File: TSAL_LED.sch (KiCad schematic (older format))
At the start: 69 parts, among them J1 Mini-SPOX, U1 XC9141, U2 XC9141

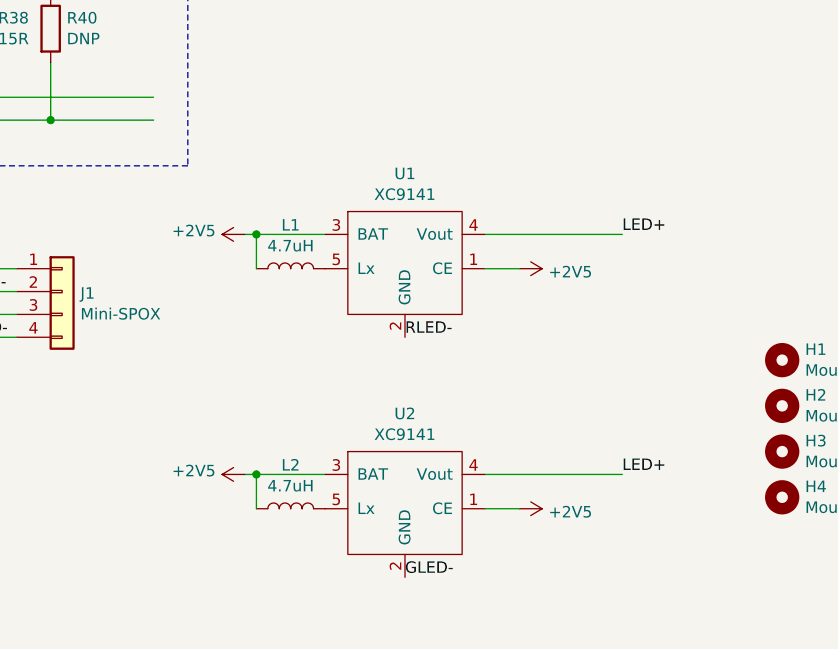
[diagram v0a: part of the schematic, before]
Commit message: remove boost converter for RLED
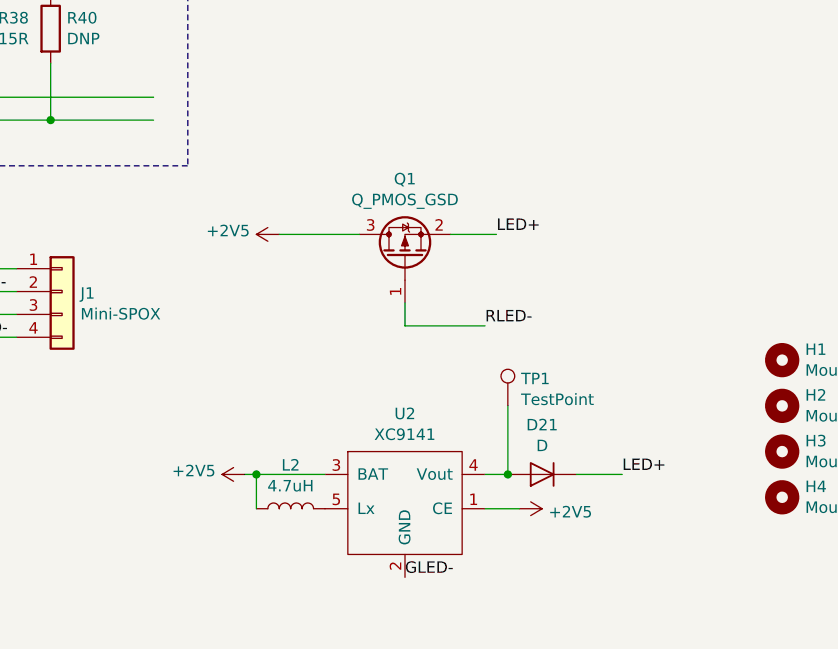
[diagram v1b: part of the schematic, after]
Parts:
- removed L1: 4.7uH, Inductor_SMD:L_Coilcraft_LPS5030, symbol Device:L
- removed U1: XC9141, Package_TO_SOT_SMD:SOT-23-5_HandSoldering, symbol xc9141:XC9141
- added D21: D, project:d0214ba, symbol Device:D
- added Q1: Q_PMOS_GSD, Package_TO_SOT_SMD:SOT-23, symbol Device:Q_PMOS_GSD
- added TP1: TestPoint, TestPoint:TestPoint_Pad_D3.0mm, symbol Connector:TestPoint
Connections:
- wire segments 146 -> 147
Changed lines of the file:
@@
-$EndComp
-$Comp
-L xc9141:XC9141 U1
-U 1 1 5E51D33E
-P 8700 4600
-F 0 "U1" H 8800 4765 50  0000 C CNN
-F 1 "XC9141" H 8800 4674 50  0000 C CNN
-F 2 "Package_TO_SOT_SMD:SOT-23-5_HandSoldering" H 8600 4700 50  0001 C CNN
-F 3 "" H 8600 4700 50  0001 C CNN
-F 4 "XC9141B33CMR-G" H 8700 4600 50  0001 C CNN "Part"
-	1    8700 4600
-	1    0    0    -1
 $EndComp
 $Comp
@@
 L power:+2V5 #PWR0101
 U 1 1 5E553241
-P 8100 4700
-F 0 "#PWR0101" H 8100 4550 50  0001 C CNN
-F 1 "+2V5" V 8115 4828 50  0000 L CNN
-F 2 "" H 8100 4700 50  0001 C CNN
-F 3 "" H 8100 4700 50  0001 C CNN
-	1    8100 4700
+P 8250 4700
+F 0 "#PWR0101" H 8250 4550 50  0001 C CNN
+F 1 "+2V5" V 8265 4828 50  0000 L CNN
+F 2 "" H 8250 4700 50  0001 C CNN
+F 3 "" H 8250 4700 50  0001 C CNN
+	1    8250 4700
 	0    -1   -1   0
 $EndComp
@@
 $EndComp
 Wire Wire Line
-	9150 4700 9750 4700
-Wire Wire Line
-	9150 5750 9750 5750
-Wire Wire Line
-	9150 4850 9300 4850
-Wire Wire Line
 	9150 5900 9300 5900
-$Comp
-L power:+2V5 #PWR0103
-U 1 1 5E58CE4F
-P 9300 4850
-F 0 "#PWR0103" H 9300 4700 50  0001 C CNN
-F 1 "+2V5" V 9315 4978 50  0000 L CNN
-F 2 "" H 9300 4850 50  0001 C CNN
-F 3 "" H 9300 4850 50  0001 C CNN
-	1    9300 4850
-	0    1    1    0
-$EndComp
 $Comp
 L power:+2V5 #PWR0104
@@
 Text Label 8800 6200 0    50   ~ 0
 GLED-
-Text Label 9750 4700 0    50   ~ 0
+Text Label 9200 4700 0    50   ~ 0
 LED+
-Text Label 8800 5150 0    50   ~ 0
-RLED-
 Text Label 9750 5750 0    50   ~ 0
 LED+
@@
 Text Label 1250 6250 0    50   ~ 0
 LED+
-$Comp
-L Device:L L1
-U 1 1 5E5F0F82
-P 8300 4850
-F 0 "L1" V 8490 4850 50  0000 C CNN
-F 1 "4.7uH" V 8399 4850 50  0000 C CNN
-F 2 "Inductor_SMD:L_Coilcraft_LPS5030" H 8300 4850 50  0001 C CNN
-F 3 "~" H 8300 4850 50  0001 C CNN
-F 4 "LTF5022T-4R7N2R0-LC" V 8300 4850 50  0001 C CNN "Part"
-	1    8300 4850
-	0    -1   -1   0
-$EndComp
 $Comp
 L Device:L L2
@@
 	8150 5750 8450 5750
 Connection ~ 8150 5750
+$Comp
+L Device:D D21
+U 1 1 5E420778
+P 9400 5750
+F 0 "D21" H 9400 5534 50  0000 C CNN
+F 1 "D" H 9400 5625 50  0000 C CNN
+F 2 "project:d0214ba" H 9400 5750 50  0001 C CNN
+F 3 "https://www.mouser.co.uk/datasheet/2/268/Microsemi_LSM115J-1592122.pdf" H 9400 5750 50  0001 C CNN
+F 4 "LSM115JE3/TR13 " H 9400 5750 50  0001 C CNN "Part"
+	1    9400 5750
+	-1   0    0    1
+$EndComp
 Wire Wire Line
-	8150 4850 8150 4700
+	9150 5750 9250 5750
 Wire Wire Line
-	8150 4700 8100 4700
+	9550 5750 9750 5750
+$Comp
+L Connector:TestPoint TP1
+U 1 1 5E44E918
+P 9250 5450
+F 0 "TP1" H 9308 5568 50  0000 L CNN
+F 1 "TestPoint" H 9308 5477 50  0000 L CNN
+F 2 "TestPoint:TestPoint_Pad_D3.0mm" H 9450 5450 50  0001 C CNN
+F 3 "~" H 9450 5450 50  0001 C CNN
+	1    9250 5450
+	1    0    0    -1
+$EndComp
 Wire Wire Line
-	8150 4700 8450 4700
-Connection ~ 8150 4700
+	9250 5450 9250 5750
+Connection ~ 9250 5750
+Wire Wire Line
+	8250 4700 8600 4700
+Wire Wire Line
+	9000 4700 9200 4700
+$Comp
+L Device:Q_PMOS_GSD Q1
+U 1 1 5E5D61D7
+P 8800 4800
+F 0 "Q1" V 9142 4800 50  0000 C CNN
+F 1 "Q_PMOS_GSD" V 9051 4800 50  0000 C CNN
+F 2 "Package_TO_SOT_SMD:SOT-23" H 9000 4900 50  0001 C CNN
+F 3 "https://www.mouser.co.uk/datasheet/2/115/DMP1045UQ-1274713.pdf" H 8800 4800 50  0001 C CNN
+F 4 "DMP1045UQ-7 " V 8800 4800 50  0001 C CNN "Part"
+	1    8800 4800
+	0    -1   -1   0
+$EndComp
+Wire Wire Line
+	8800 5000 8800 5100
+Wire Wire Line
+	8800 5100 9150 5100
+Text Label 9150 5100 0    50   ~ 0
+RLED-
 $EndSCHEMATC

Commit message: shuffled some files around, generated gerbers
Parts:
- removed D21: D, project:d0214ba, symbol Device:D
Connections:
- wire segments 147 -> 146
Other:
- moved on the sheet: Q1
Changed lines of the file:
@@
 	8150 5750 8450 5750
 Connection ~ 8150 5750
-$Comp
-L Device:D D21
-U 1 1 5E420778
-P 9400 5750
-F 0 "D21" H 9400 5534 50  0000 C CNN
-F 1 "D" H 9400 5625 50  0000 C CNN
-F 2 "project:d0214ba" H 9400 5750 50  0001 C CNN
-F 3 "https://www.mouser.co.uk/datasheet/2/268/Microsemi_LSM115J-1592122.pdf" H 9400 5750 50  0001 C CNN
-F 4 "LSM115JE3/TR13 " H 9400 5750 50  0001 C CNN "Part"
-	1    9400 5750
-	-1   0    0    1
-$EndComp
 Wire Wire Line
 	9150 5750 9250 5750
-Wire Wire Line
-	9550 5750 9750 5750
 $Comp
 L Connector:TestPoint TP1
@@
 Wire Wire Line
 	9250 5450 9250 5750
-Connection ~ 9250 5750
 Wire Wire Line
 	8250 4700 8600 4700
@@
 L Device:Q_PMOS_GSD Q1
 U 1 1 5E5D61D7
-P 8800 4800
-F 0 "Q1" V 9142 4800 50  0000 C CNN
-F 1 "Q_PMOS_GSD" V 9051 4800 50  0000 C CNN
-F 2 "Package_TO_SOT_SMD:SOT-23" H 9000 4900 50  0001 C CNN
-F 3 "https://www.mouser.co.uk/datasheet/2/115/DMP1045UQ-1274713.pdf" H 8800 4800 50  0001 C CNN
-F 4 "DMP1045UQ-7 " V 8800 4800 50  0001 C CNN "Part"
-	1    8800 4800
-	0    -1   -1   0
+P 8800 4600
+F 0 "Q1" V 9142 4600 50  0000 C CNN
+F 1 "Q_PMOS_GSD" V 9051 4600 50  0000 C CNN
+F 2 "Package_TO_SOT_SMD:SOT-23" H 9000 4700 50  0001 C CNN
+F 3 "https://www.mouser.co.uk/datasheet/2/115/DMP1045UQ-1274713.pdf" H 8800 4600 50  0001 C CNN
+F 4 "DMP1045UQ-7 " V 8800 4600 50  0001 C CNN "Part"
+	1    8800 4600
+	0    1    1    0
 $EndComp
 Wire Wire Line
-	8800 5000 8800 5100
+	8800 4400 9150 4400
+Text Label 9150 4400 0    50   ~ 0
+RLED-
 Wire Wire Line
-	8800 5100 9150 5100
-Text Label 9150 5100 0    50   ~ 0
-RLED-
+	9250 5750 9750 5750
+Connection ~ 9250 5750
 $EndSCHEMATC
